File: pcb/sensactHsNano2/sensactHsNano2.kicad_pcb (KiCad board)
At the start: 2 copper layers, 90 x 61.5 mm, 142 parts, among them J1 PROG, J2 SensactBusConnector, J3 CAN+24V, J4 HR911105A, J5 Audio, J6 Conn_01x03, J7 USB_C_Receptacle_USB2.0, J8 Conn_01x10, Q1 BC817, Q2 BC817, SW1 TERM ON, SW2 Prog, SW3 Reset, SW4 PROG_PWR, U1 TAS5805M, U10 ADS1115IDGS, U11 L78L15_SOT89, U12 SRV05, U2 LAN8720A, U3 ESP32, U4 DS2482, U5 SN65HVD230, U6 CH340K, U7 MP4420, U8 LM358, U9 MCP4728, X1 50MHz

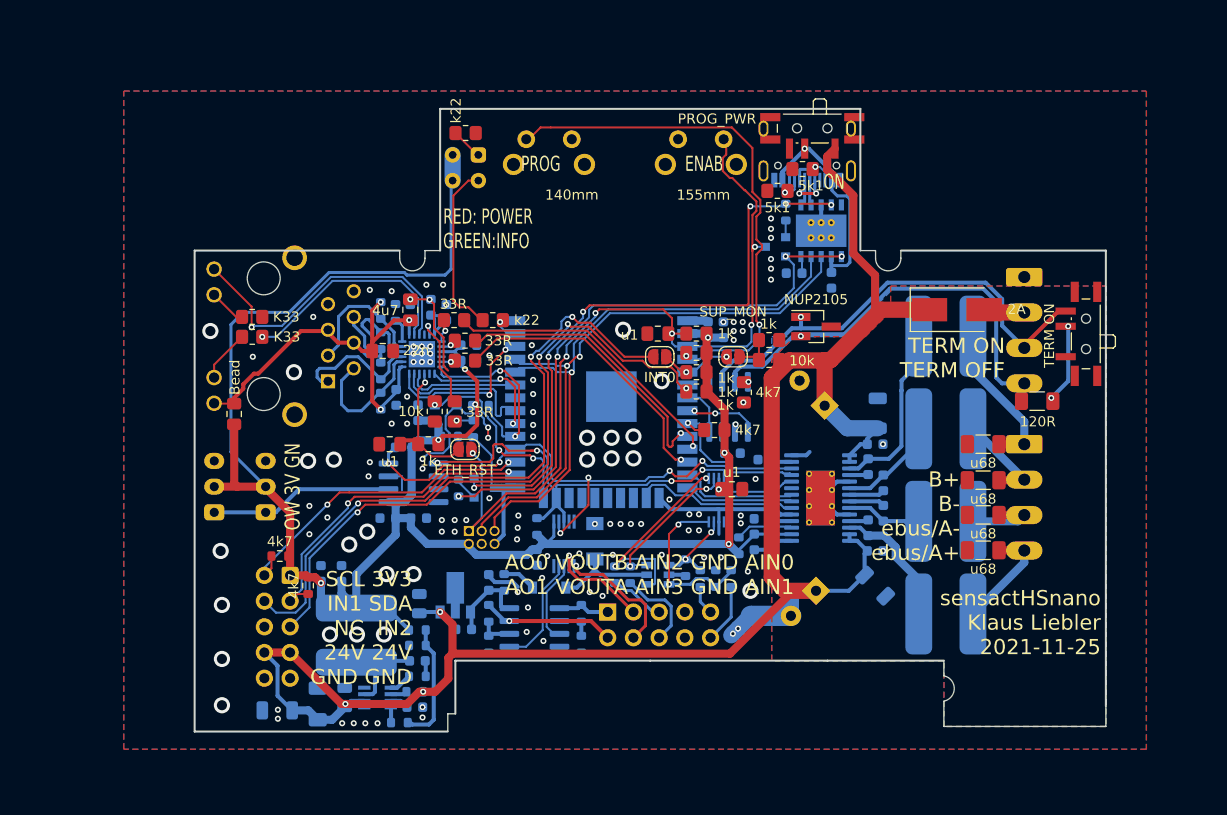
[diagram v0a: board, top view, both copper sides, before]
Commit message: sensactHsNano & sensactHsRelay
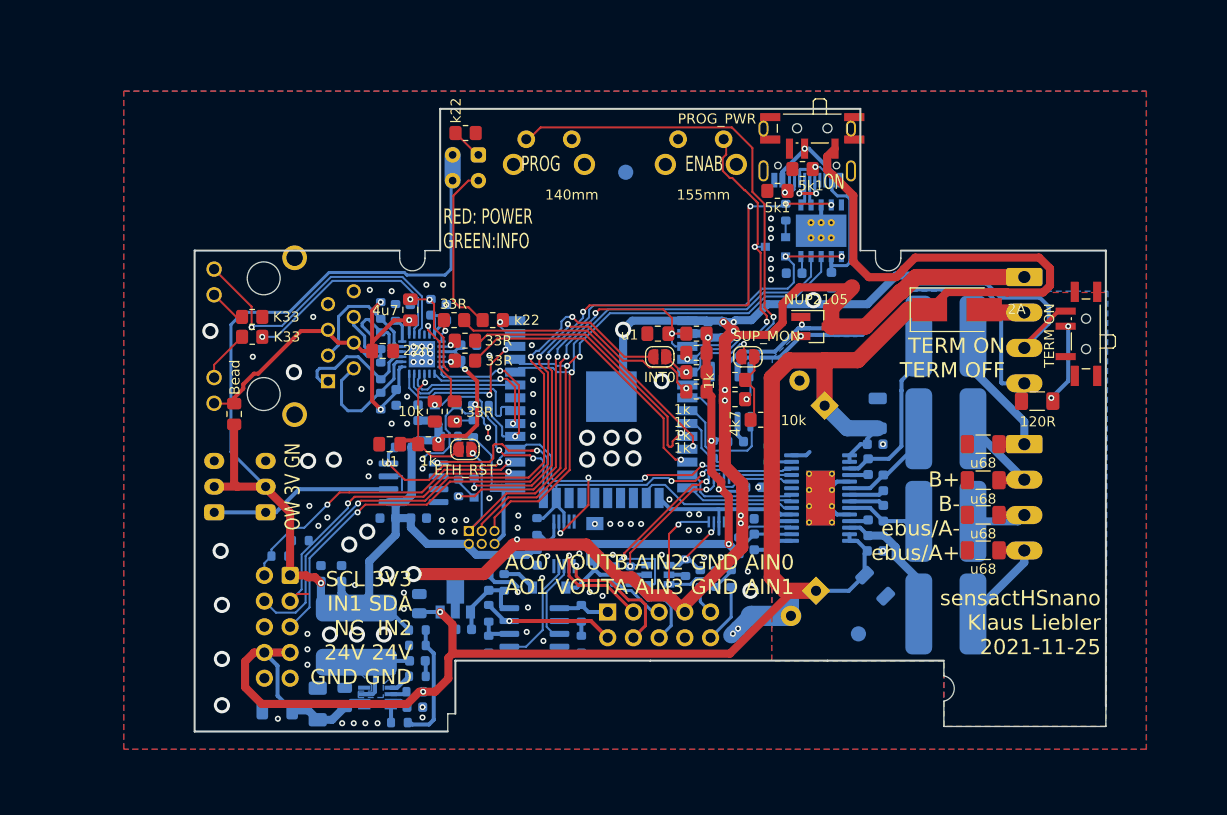
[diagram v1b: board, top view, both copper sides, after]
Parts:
- added FID1: Fiducial, Fiducial:Fiducial_1.5mm_Mask3mm, B.Cu at (170.6, 145.6)
- added FID2: Fiducial, Fiducial:Fiducial_1.5mm_Mask3mm, B.Cu at (147.6, 100.0)
- C48: footprint Capacitor_SMD:C_0805_2012Metric_Pad1.18x1.45mm_HandSolder -> Capacitor_SMD:C_0603_1608Metric; moved to B.Cu
- R1, R6: moved to B.Cu
- R2: footprint Resistor_SMD:R_0805_2012Metric_Pad1.20x1.40mm_HandSolder -> Resistor_SMD:R_0603_1608Metric; moved to B.Cu
- moved R44 5.96 mm to (160.9, 124.5)
- moved R45 5.18 mm to (158.4, 120.5), turned to 180 degrees
- moved R1 4.51 mm to (115.4, 136.4), turned to 0 degrees
- moved C48 2.17 mm to (160.2, 131.1)
- moved R2 1.91 mm to (156.2, 127.4), turned to 270 degrees
- moved JP2 1.46 mm to (159.6, 118.2)
- moved C22 1.19 mm to (158.4, 126.6)
- moved R3 1.11 mm to (158.4, 122.4), turned to 180 degrees
- moved U5 1.05 mm to (158.0, 122.2)
- moved C6 0.63 mm to (161.7, 127.8), turned to 90 degrees
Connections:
- net Net-(C37-Pad1) renamed /psu/SW
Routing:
- net GND: track 59.0 -> 214.3 mm, vias 122 -> 125
- net +24V: track 171.9 -> 210.8 mm, vias 3 -> 2
- net +3V3: track 215.7 -> 223.9 mm
- net CANL: track 44.8 -> 50.2 mm
- net CAN_TX: track 7.42 -> 12.0 mm, vias 2 -> 0
- net SENSOR_VN: track 7.87 -> 11.9 mm
- net SUPPLY_MONITOR: track 4.01 -> 7.12 mm
- net Net-(R3-Pad1): track 0.00 -> 3.03 mm
- net AMP_PDN: track 15.5 -> 13.4 mm, vias 1 -> 0
- net SCL1: track 31.4 -> 29.8 mm
- net SCL2: track 58.2 -> 56.9 mm
- net /psu/SW: track 12.2 -> 10.9 mm
- net CAN_RX: track 4.97 -> 3.86 mm
- net /VINC: track 20.4 -> 19.7 mm
- net CANH: track 44.2 -> 43.6 mm
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- added copper zone on B.Cu, net /psu/SW

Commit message: Various
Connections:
- J2 pad 6: Net-(J2-Pad6) -> unconnected-(J2-Pad6)
- J7 pad A8: Net-(J7-PadA8) -> unconnected-(J7-PadA8)
- J7 pad B8: Net-(J7-PadB8) -> unconnected-(J7-PadB8)
- SW1 pad 1: Net-(SW1-Pad1) -> unconnected-(SW1-Pad1)
- SW4 pad 3: Net-(SW4-Pad3) -> unconnected-(SW4-Pad3)
- U1 pad 9: Net-(U1-Pad9) -> unconnected-(U1-Pad9)
- U10 pad 1: Net-(U10-Pad1) -> unconnected-(U10-Pad1)
- U10 pad 2: Net-(U10-Pad2) -> unconnected-(U10-Pad2)
- U2 pad 10: Net-(U2-Pad10) -> unconnected-(U2-Pad10)
- U2 pad 14: Net-(U2-Pad14) -> unconnected-(U2-Pad14)
- U2 pad 4: Net-(U2-Pad4) -> unconnected-(U2-Pad4)
- U3 pad 17: Net-(U3-Pad17) -> unconnected-(U3-Pad17)
- U3 pad 18: Net-(U3-Pad18) -> unconnected-(U3-Pad18)
- U3 pad 19: Net-(U3-Pad19) -> unconnected-(U3-Pad19)
- U3 pad 20: Net-(U3-Pad20) -> unconnected-(U3-Pad20)
- U3 pad 21: Net-(U3-Pad21) -> unconnected-(U3-Pad21)
- U3 pad 22: Net-(U3-Pad22) -> unconnected-(U3-Pad22)
- U3 pad 32: Net-(U3-Pad32) -> unconnected-(U3-Pad32)
- U4 pad 6: Net-(U4-Pad6) -> unconnected-(U4-Pad6)
- U5 pad 5: Net-(U5-Pad5) -> unconnected-(U5-Pad5)
- U6 pad 5: Net-(U6-Pad5) -> unconnected-(U6-Pad5)
- U7 pad 1: Net-(U7-Pad1) -> unconnected-(U7-Pad1)
- U9 pad 4: Net-(U9-Pad4) -> unconnected-(U9-Pad4)
- U9 pad 5: Net-(U9-Pad5) -> unconnected-(U9-Pad5)
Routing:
- net +3V3: track 223.9 -> 213.0 mm
- net GND: track 214.3 -> 209.3 mm
- net OUT_B+: track 15.3 -> 11.9 mm
- net Net-(C11-Pad1): track 12.9 -> 9.53 mm
- net Net-(C12-Pad1): track 8.86 -> 6.00 mm
- net Net-(C13-Pad1): track 17.6 -> 14.9 mm
- net SDA2: track 51.1 -> 48.4 mm
- net CANH: track 43.6 -> 41.1 mm
- net Net-(D4-Pad2): track 5.94 -> 3.58 mm
- net SENSOR_VN: track 11.9 -> 9.61 mm
- net /psu/SW: track 10.9 -> 8.64 mm
- net CANL: track 50.2 -> 48.0 mm
- net GNDA: track 11.1 -> 8.99 mm
- net SDA1: track 31.7 -> 29.6 mm
- net /eth/VDD2A: track 47.8 -> 46.0 mm
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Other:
- outline, holes or cut-outs redrawn
- net class Default removed
- net class HigherVoltage removed

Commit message: Sicherung
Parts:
- moved J7 47.5 mm to (119.9, 110.1)
- moved J6 16.2 mm to (112.0, 117.4)
- moved J4 10.3 mm to (111.9, 126.5)
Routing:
- net GND: vias 125 -> 122
- net /eth/VDD2A: vias 3 -> 4
- net /eth/RX_P: vias 0 -> 1
- net +3V3: vias 8 -> 9
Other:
- board size 90 x 61.5 mm -> 90 x 50 mm

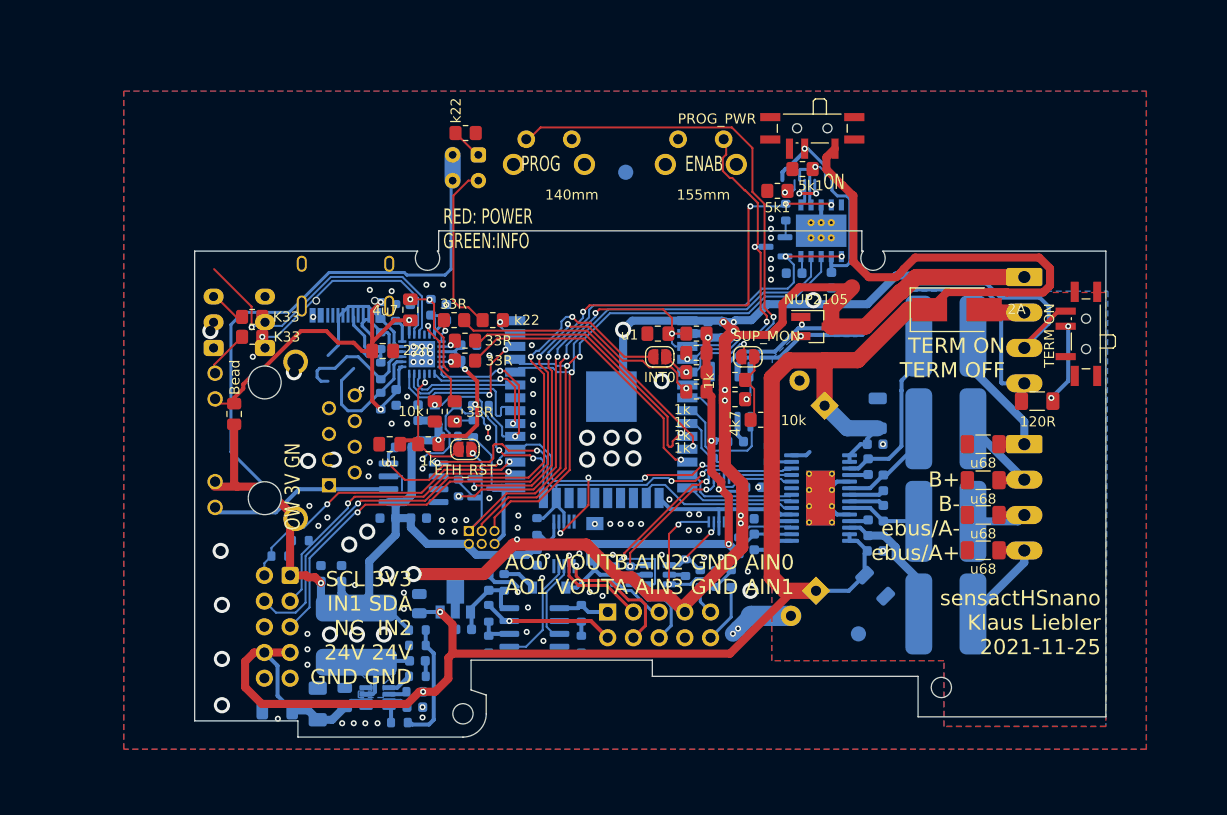
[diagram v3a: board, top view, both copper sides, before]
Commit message: DIn-schiene-seitenwand + sensactHsNano2
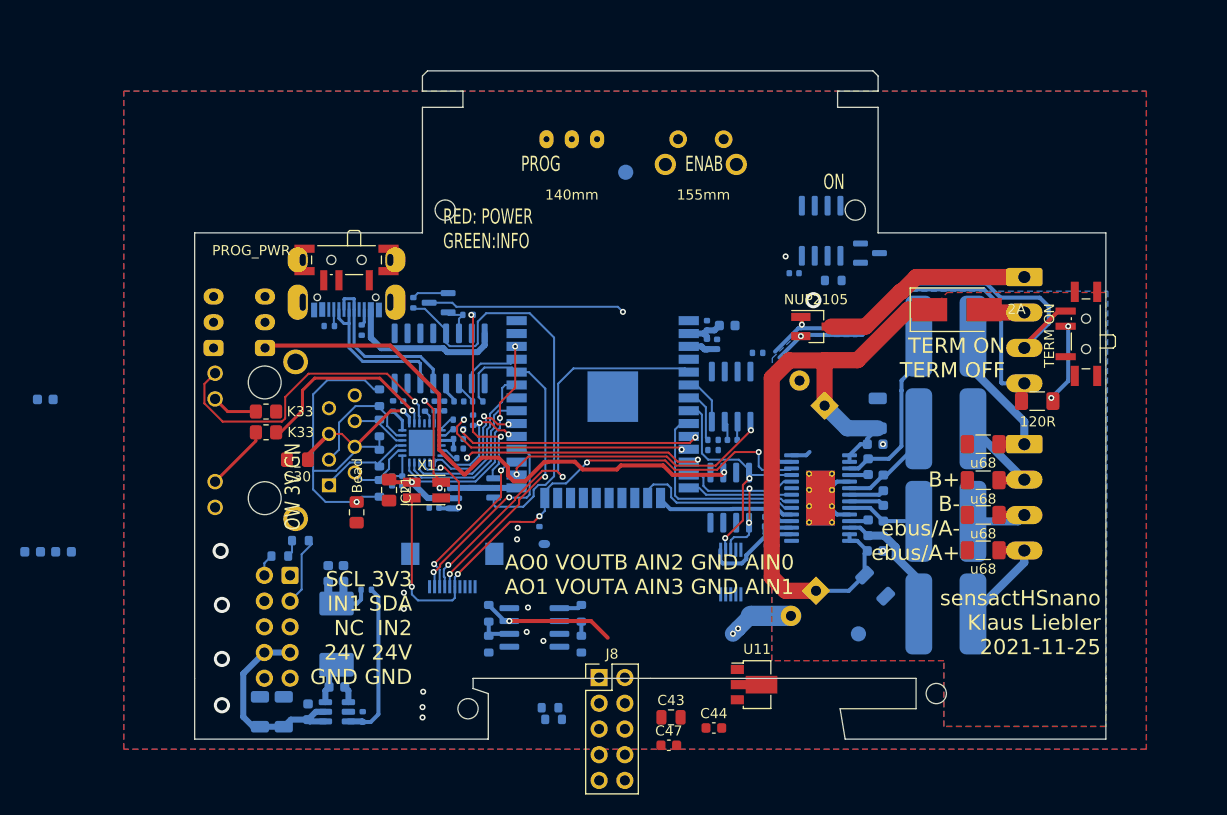
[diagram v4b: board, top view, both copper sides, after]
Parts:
- removed C46, C48: u1, Capacitor_SMD:C_0603_1608Metric
- removed D2: 1N4, Diode_SMD:D_SOD-123
- removed D5: 3V3, Diode_SMD:D_MiniMELF
- removed JP1: INT0, Jumper:SolderJumper-2_P1.3mm_Open_RoundedPad1.0x1.5mm
- removed JP2: SUP_MON, Jumper:SolderJumper-2_P1.3mm_Open_RoundedPad1.0x1.5mm
- removed JP3: ETH_RST, Jumper:SolderJumper-2_P1.3mm_Open_RoundedPad1.0x1.5mm
- removed R2, R29: 4k7, Resistor_SMD:R_0603_1608Metric
- removed R34: 12k1, Resistor_SMD:R_0603_1608Metric
- removed R35: 39k, Resistor_SMD:R_0603_1608Metric
- removed R36: 1k, Resistor_SMD:R_0603_1608Metric
- removed R37, R39, R49, R53: 22k, Resistor_SMD:R_0603_1608Metric
- removed R38, R40: 10k, Resistor_SMD:R_0603_1608Metric
- removed R42: 10k, Resistor_SMD:R_0805_2012Metric_Pad1.20x1.40mm_HandSolder
- removed R43, R46: 1k, Resistor_SMD:R_0805_2012Metric_Pad1.20x1.40mm_HandSolder
- removed U10: ADS1115IDGS, Package_SO:TSSOP-10_3x3mm_P0.5mm
- removed U12: SRV05, Package_TO_SOT_SMD:SOT-23-6
- added U13: CH340C, Package_SO:SOIC-16_3.9x9.9mm_P1.27mm, B.Cu at (129.2, 118.4)
- C2, C22, C23, C24, C25, C26, C27, C28, C32, C4, C41, C42, C6, C7: footprint Capacitor_SMD:C_0603_1608Metric -> Capacitor_SMD:C_0402_1005Metric
- C21: footprint Capacitor_SMD:C_0603_1608Metric -> Capacitor_SMD:C_0805_2012Metric_Pad1.18x1.45mm_HandSolder; moved to F.Cu
- C29, C40, C45: footprint Capacitor_SMD:C_0805_2012Metric_Pad1.18x1.45mm_HandSolder -> Capacitor_SMD:C_0402_1005Metric; moved to B.Cu
- C31: value 10u -> u1; footprint Capacitor_SMD:C_1206_3216Metric -> Capacitor_SMD:C_0603_1608Metric
- C34: footprint Capacitor_SMD:C_1206_3216Metric_Pad1.33x1.80mm_HandSolder -> Capacitor_SMD:C_1206_3216Metric
- C35: value u1 -> 10u; footprint Capacitor_SMD:C_0805_2012Metric -> Capacitor_SMD:C_1206_3216Metric
- C43, C44, C47, J8, U11: moved to F.Cu
- D1: value Rpower_Ginfo -> PSM712; footprint liebler_SEMICONDUCTORS:Dialight-5530123F-0 -> Package_TO_SOT_SMD:SOT-23
- J1: value PROG -> HMI; footprint liebler_CONN:IDC_2x03_P1.27mm_Vertical -> Connector_FFC-FPC:Hirose_FH12-10S-0.5SH_1x10-1MP_P0.50mm_Horizontal
- J7: value USB_C_Receptacle_USB2.0 -> PROG; footprint Connector_USB:USB_C_Receptacle_HRO_TYPE-C-31-M-12 -> liebler_CONN:USB_C_Receptacle_HRO_TYPE-C-31-M-12_IMPROVED
- L5: value 10uH -> 4u7; footprint liebler_PASSIVES:ASPIAIG-Q8080 -> Inductor_SMD:L_Abracon_ASPI-0630LR
- R10, R11, R12, R14, R3, R30, R44, R45, R9: footprint Resistor_SMD:R_0805_2012Metric_Pad1.20x1.40mm_HandSolder -> Resistor_SMD:R_0402_1005Metric; moved to B.Cu
- R13: footprint Resistor_SMD:R_0805_2012Metric_Pad1.20x1.40mm_HandSolder -> Resistor_SMD:R_0603_1608Metric; moved to B.Cu
- R16, R25, R32, R4, R5, R8: footprint Resistor_SMD:R_0603_1608Metric -> Resistor_SMD:R_0402_1005Metric
- R22: value 1M -> 1k
- R23: value 51k -> K12
- R24: value 22R -> 47k; footprint Resistor_SMD:R_0603_1608Metric -> Resistor_SMD:R_0402_1005Metric
- R26: value k22 -> 15k; footprint Resistor_SMD:R_0805_2012Metric_Pad1.20x1.40mm_HandSolder -> Resistor_SMD:R_0402_1005Metric; moved to B.Cu
- R27: value k22 -> 5k1; footprint Resistor_SMD:R_0805_2012Metric_Pad1.20x1.40mm_HandSolder -> Resistor_SMD:R_0402_1005Metric; moved to B.Cu
- R28: value 4k7 -> 1k; footprint Resistor_SMD:R_0603_1608Metric -> Resistor_SMD:R_0402_1005Metric
- R31: value 5k1 -> 10k; footprint Resistor_SMD:R_0805_2012Metric_Pad1.20x1.40mm_HandSolder -> Resistor_SMD:R_0402_1005Metric; moved to B.Cu
- R33: value 10k -> 4k7; footprint Resistor_SMD:R_0603_1608Metric -> Resistor_SMD:R_0402_1005Metric
- R47: value 1k -> 4k7; footprint Resistor_SMD:R_0805_2012Metric_Pad1.20x1.40mm_HandSolder -> Resistor_SMD:R_0402_1005Metric; moved to B.Cu
- SW2: value Prog -> OFF TERM ON; footprint Button_Switch_THT:SW_Tactile_SPST_Angled_PTS645Vx58-2LFS -> liebler_MECH:Switch_SS12D00
- U6: value CH340K -> MAX3485; footprint liebler_SEMICONDUCTORS:SSOP-10_3.9x4.9mm_P1.00mm_EP -> Package_SO:SOIC-8_3.9x4.9mm_P1.27mm
- U7: value MP4420 -> RY8310; footprint Package_TO_SOT_SMD:TSOT-23-8 -> Package_TO_SOT_SMD:SOT-23-6
- X1: footprint Oscillator:Oscillator_SMD_EuroQuartz_XO32-4Pin_3.2x2.5mm -> Oscillator:Oscillator_SMD_EuroQuartz_XO32-4Pin_3.2x2.5mm_HandSoldering; moved to F.Cu
- moved SW4 47.8 mm to (120.0, 109.0)
- moved R30 43.3 mm to (121.5, 115.6), turned to 90 degrees
- moved R26 41.2 mm to (121.6, 153.8), turned to -90 degrees
- moved D1 41.2 mm to (171.7, 108.0)
- moved R33 39.1 mm to (139.1, 134.5), turned to -90 degrees
- moved C41 38.7 mm to (131.1, 122.7), turned to 0 degrees
- moved C31 38.3 mm to (90.2, 122.5)
- moved R31 36.0 mm to (132.0, 114.1), turned to 180 degrees
- moved C19 35.2 mm to (92.0, 137.5)
- moved C20 35.2 mm to (89.0, 137.5)
- moved Q2 33.7 mm to (129.1, 112.9)
- moved U4 31.3 mm to (157.8, 132.2), turned to -90 degrees
- moved U11 30.8 mm to (160.2, 150.6), turned to 0 degrees
- moved C43 27.3 mm to (152.1, 153.8), turned to 0 degrees
- moved C44 26.6 mm to (156.3, 154.9)
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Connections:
- net LRCLK renamed I2S_LRCLK
- net Net-(C23-Pad1) renamed /eth/VDDCR
- net Net-(C45-Pad1) renamed /eth/RST
- net Net-(R16-Pad2) renamed /eth/RBIAS
- C31 pad 2: +24V -> +3V3
- C36 pad 2: Net-(C36-Pad2) -> +24V
- C37 pad 1: /psu/SW -> Net-(C37-Pad1)
- C37 pad 2: Net-(C37-Pad2) -> /psu/SW
- C40 pad 1: EN -> PROG_EN
- C41 pad 1: V_BUS_USB -> Net-(C41-Pad1)
- C42 pad 1: GND -> +5P
- C42 pad 2: Net-(C42-Pad2) -> GND
- D1 pad 1: Net-(D1-Pad1) -> RS485A
- D1 pad 2: +3V3 -> RS485B
- D1 pad 3: Net-(D1-Pad3) -> GND
- J1 pad 1: EN -> BUZZER
- J1 pad 2: +3V3 -> MOSI
- J1 pad 3: PROG_TX -> SCLK
- J1 pad 4: GND -> SW1
- J1 pad 5: PROG_RX -> RS
- J1 pad 6: ETH_CLK -> AMP_PDN
- J7 pad A4: V_BUS_USB -> +5P
- J7 pad A6: Net-(J7-PadA6) -> /prog/UD+
- J7 pad A7: Net-(J7-PadA7) -> /prog/UD-
- J7 pad A9: V_BUS_USB -> +5P
- J7 pad B4: V_BUS_USB -> +5P
- J7 pad B6: Net-(J7-PadA6) -> /prog/UD+
- J7 pad B7: Net-(J7-PadA7) -> /prog/UD-
- J7 pad B9: V_BUS_USB -> +5P
- Q2 pad 3: EN -> PROG_EN
- R11 pad 2: EN -> PROG_EN
- R13 pad 1: +3V3 -> RS485B
- R13 pad 2: /ProgBTN -> GND
- R22 pad 1: +24V -> +3V3
- R22 pad 2: Net-(R22-Pad2) -> RS485A
- R23 pad 1: Net-(R23-Pad1) -> RS485A
- R24 pad 1: Net-(C37-Pad2) -> +3V3
- R26 pad 1: Net-(D1-Pad3) -> GND
- R26 pad 2: Net-(R26-Pad2) -> Net-(R24-Pad2)
- R27 pad 1: Net-(D1-Pad1) -> GND
- R27 pad 2: GND -> Net-(J7-PadA5)
- R28 pad 1: +3V3 -> PROG_RX
- R28 pad 2: SDA2 -> RS
- R30 pad 2: Net-(J7-PadA5) -> Net-(J7-PadB5)
- R31 pad 1: GND -> Net-(Q1-Pad1)
- R31 pad 2: Net-(J7-PadB5) -> /prog/RTS
- R32 pad 1: Net-(Q1-Pad1) -> Net-(Q2-Pad1)
- R32 pad 2: /prog/RTS -> /prog/DTR
- R33 pad 1: Net-(Q2-Pad1) -> AMP_PDN
- R33 pad 2: /prog/DTR -> GND
- SW2 pad 1: GND -> unconnected-(SW2-Pad1)
- SW2 pad 2: /ProgBTN -> RS485B
- SW3 pad 1: EN -> PROG_EN
- U1 pad 10: SDA2 -> SDA1
- U1 pad 11: SCL2 -> SCL1
- U1 pad 7: SCLK -> I2S_SCLK
- U1 pad 8: SDIN -> I2S_SDAT
- U3 pad 13: SDIN -> SDA1
- U3 pad 14: SCLK -> I2S_SDAT
- U3 pad 23: SDA2 -> unconnected-(U3-Pad23)
- U3 pad 24: ETH_POWER -> AMP_PDN
- U3 pad 26: SDA1 -> CAN_TX
- U3 pad 27: SCL1 -> SCLK
- U3 pad 28: SCL2 -> MOSI
- U3 pad 3: EN -> PROG_EN
- U3 pad 34: PROG_RX -> RS
- U3 pad 37: Net-(R26-Pad2) -> 485_DI
- U3 pad 4: /ProgBTN -> 485_RO
- U3 pad 5: SENSOR_VN -> SW1
- U3 pad 6: INT1 -> CAN_RX
- U3 pad 7: CAN_RX -> SUPPLY_MONITOR
- U3 pad 8: CAN_TX -> SCL1
- U3 pad 9: AMP_PDN -> I2S_SCLK
- U4 pad 4: SCL2 -> SCL1
- U4 pad 5: SDA2 -> SDA1
- U6 pad 1: Net-(J7-PadA6) -> 485_RO
- U6 pad 2: Net-(J7-PadA7) -> 485_DE
- U6 pad 3: GND -> 485_DE
- U6 pad 4: /prog/DTR -> 485_DI
- U6 pad 5: unconnected-(U6-Pad5) -> GND
- U6 pad 6: /prog/RTS -> RS485A
- U6 pad 7: V_BUS_USB -> RS485B
- U6 pad 8: PROG_TX -> +3V3
- U7 pad 1: unconnected-(U7-Pad1) -> Net-(C37-Pad1)
- U7 pad 2: +24V -> GND
- U7 pad 3: /psu/SW -> Net-(R24-Pad2)
- U7 pad 4: GND -> +24V
- U7 pad 5: Net-(R24-Pad2) -> +24V
- U7 pad 6: Net-(R22-Pad2) -> /psu/SW
- U8 pad 4: GND -> (no net)
- U8 pad 8: +15V -> (no net)
- U9 pad 2: SCL2 -> SCL1
- U9 pad 3: SDA2 -> SDA1
- X1 pad 1: ETH_POWER -> AMP_PDN
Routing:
- net +3V3: track 213.0 -> 37.1 mm, vias 9 -> 1
- net GND: track 209.3 -> 39.2 mm, vias 122 -> 2
- net +24V: track 209.8 -> 89.9 mm, vias 2 -> 0
- net EN: track 80.8 -> 0.00 mm, vias 6 -> 0
- net INT1: track 65.3 -> 0.00 mm, vias 4 -> 0
- net INT0: track 63.7 -> 0.00 mm, vias 3 -> 0
- net SCL2: track 55.5 -> 0.00 mm, vias 6 -> 0
- net PROG_RX: track 57.1 -> 2.33 mm, vias 1 -> 0
- net /prog/RTS: track 57.5 -> 3.74 mm, vias 4 -> 0
- net PROG_TX: track 58.1 -> 5.91 mm, vias 2 -> 0
- net /ProgBTN: track 50.9 -> 0.00 mm, vias 2 -> 0
- net SDA2: track 48.4 -> 0.00 mm, vias 4 -> 0
- net AMP_PDN: track 12.4 -> 58.1 mm, vias 0 -> 5
- net SW1: track 0.00 -> 40.9 mm, vias 0 -> 2
- net OneWire: track 18.2 -> 57.9 mm, vias 0 -> 1
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- added copper zone on B.Cu, net (none)
- added copper zone on F.Cu, net (none)
- removed copper zone on B.Cu, net /psu/SW
- removed copper zone on B.Cu, net GND
- removed copper zone on F.Cu, net GND
- removed copper zone on B.Cu, net GNDA
- removed copper zone on F.Cu, net GNDA
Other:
- board size 90 x 50 mm -> 90 x 66 mm

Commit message: sensactNanoHS2
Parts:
- removed D4: 2A, Diode_SMD:D_SMB_Handsoldering
- removed FID1, FID2: Fiducial, Fiducial:Fiducial_1.5mm_Mask3mm
- added C46: u1, Capacitor_SMD:C_0402_1005Metric, B.Cu at (149.9, 143.4)
- added D2: 2A, Diode_SMD:D_SMB_Handsoldering, F.Cu at (179.9, 143.8)
- added J9: 24V, Connector_Phoenix_MC:PhoenixContact_MC_1,5_2-G-3.81_1x02_P3.81mm_Horizontal, B.Cu at (186.9, 143.7)
- C19, C20, C31: footprint Capacitor_SMD:C_0603_1608Metric -> Capacitor_SMD:C_0402_1005Metric
- C43, FB1: moved to B.Cu
- C44, C47: footprint Capacitor_SMD:C_0603_1608Metric -> Capacitor_SMD:C_0402_1005Metric; moved to B.Cu
- D1: footprint Package_TO_SOT_SMD:SOT-23 -> Package_TO_SOT_SMD:SOT-23_Handsoldering; moved to F.Cu
- J3: value CAN+24V -> CAN+485
- R23: footprint Resistor_SMD:R_0603_1608Metric -> Resistor_SMD:R_0805_2012Metric_Pad1.20x1.40mm_HandSolder; moved to F.Cu
- R41, R48, R51, R52: footprint Resistor_SMD:R_0603_1608Metric -> Resistor_SMD:R_0402_1005Metric
- SW2: footprint liebler_MECH:Switch_SS12D00 -> liebler_MECH:SW_SPDT_PCM12_handsolder; moved to F.Cu
- SW3: footprint Button_Switch_THT:SW_Tactile_SPST_Angled_PTS645Vx58-2LFS -> liebler_MECH:Button_2x4x3,5_handsolder; moved to F.Cu
- U1: footprint Package_SO:HTSSOP-28-1EP_4.4x9.7mm_P0.65mm_EP2.85x5.4mm_ThermalVias -> liebler_SEMICONDUCTORS:TSSOP-28_4.4x9.7mm_Pitch0.65mm_pad_handsolder
- U11: footprint Package_TO_SOT_SMD:SOT-89-3 -> Package_TO_SOT_SMD:SOT-89-3_Handsoldering; moved to B.Cu
- moved C31 79.3 mm to (169.1, 114.3), turned to 180 degrees
- moved C20 69.8 mm to (158.1, 127.5), turned to 0 degrees
- moved R23 65.7 mm to (187.6, 108.3), turned to 0 degrees
- moved C19 56.1 mm to (148.1, 134.7), turned to -90 degrees
- moved SW2 52.5 mm to (192.7, 111.3), turned to 90 degrees
- moved R22 49.8 mm to (168.9, 112.3), turned to 90 degrees
- moved SW3 48.4 mm to (110.2, 108.1), turned to 0 degrees
- moved C42 41.3 mm to (123.4, 116.6), turned to 90 degrees
- moved U11 30.8 mm to (129.9, 145.3), turned to 180 degrees
- moved C44 24.4 mm to (134.5, 143.8), turned to 180 degrees
- moved C47 22.2 mm to (155.2, 134.7), turned to -90 degrees
- moved C43 19.2 mm to (134.5, 146.1), turned to 90 degrees
- moved R48 16.5 mm to (159.4, 143.7), turned to 90 degrees
- moved R51 16.0 mm to (149.9, 145.3)
- moved R41 15.9 mm to (149.9, 147.2)
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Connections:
- J3 pad 1: GND -> RS485A
- J3 pad 2: Net-(D4-Pad2) -> RS485B
- J8 pad 3: /VOUTB -> /VOUTD
- J8 pad 4: /VOUTA -> /VOUTC
- SW3 pad 1: PROG_EN -> GND
- SW3 pad 2: GND -> PROG_EN
- SW4 pad 2: V_BUS_USB -> +5P
- U3 pad 23: unconnected-(U3-Pad23) -> 485_DE
- U3 pad 26: CAN_TX -> MOSI
- U3 pad 27: SCLK -> CAN_TX
- U3 pad 28: MOSI -> SCLK
- U8 pad 3: /VOUTC -> /VOUTA
- U8 pad 4: (no net) -> GND
- U8 pad 5: /VOUTD -> /VOUTB
- U8 pad 8: (no net) -> +15V
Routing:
- net +3V3: track 37.1 -> 185.1 mm, vias 1 -> 11
- net +24V: track 89.9 -> 232.1 mm, vias 0 -> 2
- net GND: track 39.2 -> 108.3 mm, vias 2 -> 29
- net SCL1: track 26.1 -> 77.4 mm
- net SDA1: track 26.4 -> 77.7 mm
- net 485_DE: track 0.00 -> 43.1 mm, vias 0 -> 2
- net GNDA: track 8.99 -> 51.9 mm, vias 2 -> 0
- net RS485B: track 0.00 -> 32.0 mm, vias 0 -> 1
- net PROG_EN: track 22.7 -> 54.4 mm, vias 1 -> 3
- net 485_DI: track 0.00 -> 26.8 mm, vias 0 -> 2
- net RS485A: track 0.00 -> 22.8 mm, vias 0 -> 1
- net +15V: track 0.00 -> 22.7 mm, vias 0 -> 2
- net /VOUTC: track 0.00 -> 18.3 mm
- net /VOUTD: track 0.00 -> 16.0 mm
- net /VOUTB: track 0.00 -> 13.6 mm
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- added copper zone on B.Cu, net +24V
- added copper zone on B.Cu, net /psu/SW
- added copper zone on B.Cu, net GND
- added copper zone on F.Cu, net GND
- added copper zone on B.Cu, net GNDA
- added copper zone on F.Cu, net GNDA
- removed copper zone on B.Cu, net (none)
- removed copper zone on F.Cu, net (none)
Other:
- board size 90 x 66 mm -> 90 x 54.8 mm
